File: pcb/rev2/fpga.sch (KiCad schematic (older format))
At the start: 45 parts, among them CN4 JTAG, IC1 XC6SLX9-3TQG144I, IC2 M25P80-VMN6P

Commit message: pcb wip
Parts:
- C10, C12, C13, C14, C15, C16, C18, C19, C20, C21, C22, C23, C24, C25, C3, C35, C36, C37, C38, C4, C40, C5, C6, C8, C9: footprint CAPC1608X87N -> Capacitors SMD:CAPC1608X87N
- C26, C39: footprint CAPC1608X90N -> Capacitors SMD:CAPC1608X90N
- R10, R11, R12, R13, R14, R15, R16, R17, R18, R20, R21, R7, R72, R8, R9: footprint RESC1608X55N -> Resistors SMD:RESC1608X55N

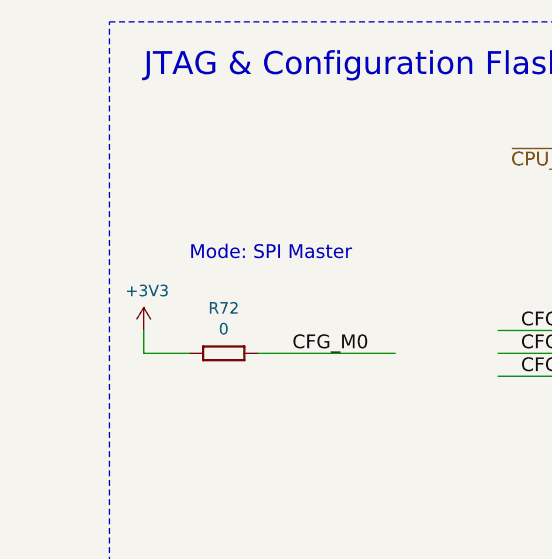
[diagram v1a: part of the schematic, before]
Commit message: Completed port to KiCad, passes DRC+LVS. NOT MANUFACTURED.
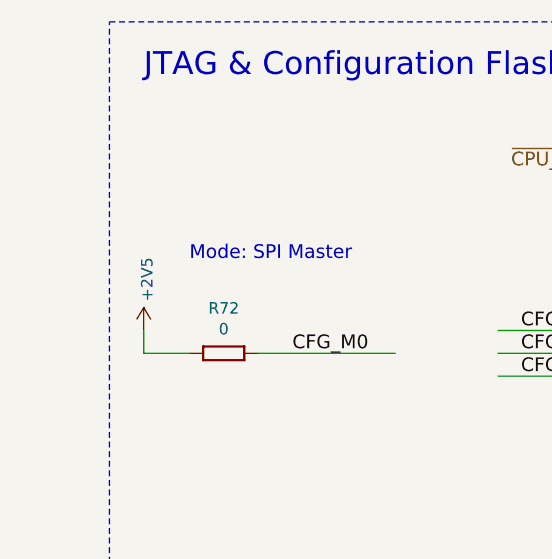
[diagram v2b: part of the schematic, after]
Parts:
- CN4: footprint (none) -> Pin_Headers:Pin_Header_Straight_1x06; Fieldname (none) -> Value
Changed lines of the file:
@@
 F 0 "CN4" H 6469 2175 50  0000 C CNN
 F 1 "JTAG" H 6469 2266 50  0000 C CNN
-F 2 "" H 6550 2650 50  0001 C CNN
+F 2 "Pin_Headers:Pin_Header_Straight_1x06" H 6550 2650 50  0001 C CNN
 F 3 "" H 6550 2650 50  0001 C CNN
+F 4 "Value" H 6550 2650 60  0001 C CNN "Fieldname"
 	1    6550 2650
 	-1   0    0    1
@@
 	1    0    0    -1
 $EndComp
-$Comp
-L +3V3 #PWR019
-U 1 1 5990096E
-P 1450 2250
-F 0 "#PWR019" H 1450 2100 50  0001 C CNN
-F 1 "+3V3" H 1465 2423 50  0000 C CNN
-F 2 "" H 1450 2250 50  0001 C CNN
-F 3 "" H 1450 2250 50  0001 C CNN
-	1    1450 2250
-	1    0    0    -1
-$EndComp
 Text Notes 1650 1950 0    60   ~ 0
 Mode: SPI Master
@@
 Text Notes 12450 10925 2    60   ~ 0
 FPGA
+$Comp
+L +2V5 #PWR019
+U 1 1 599ECA35
+P 1450 2250
+F 0 "#PWR019" H 1450 2100 50  0001 C CNN
+F 1 "+2V5" V 1465 2378 50  0000 L CNN
+F 2 "" H 1450 2250 50  0001 C CNN
+F 3 "" H 1450 2250 50  0001 C CNN
+	1    1450 2250
+	1    0    0    -1
+$EndComp
 $EndSCHEMATC

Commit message: axi4/zynq version: wip
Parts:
- C10, C12, C13, C15, C16, C18, C20, C21, C22, C23, C25, C3, C35, C36, C37, C38, C4, C40, C5, C8: symbol CC0603_100NF_50V_10%_X7R -> dsi_shield-rescue:CC0603_100NF_50V_10%_X7R-
- C14, C19, C24, C6, C9: symbol CC0603_1UF_50V_10%_X5R -> dsi_shield-rescue:CC0603_1UF_50V_10%_X5R-
- C26, C39: symbol CC0603_1NF_50V_5%_NP0 -> dsi_shield-rescue:CC0603_1NF_50V_5%_NP0-
- CN4: symbol CONN_01X06 -> dsi_shield-rescue:CONN_01X06-
- IC1: symbol XC6SLX9-3TQG144I -> dsi_shield-rescue:XC6SLX9-3TQG144I-
- IC2: symbol M25P80-VMN6P -> dsi_shield-rescue:M25P80-VMN6P-
- R10, R7, R8, R9: symbol R0603_3K3_1%_0.1W_100PPM -> dsi_shield-rescue:R0603_3K3_1%_0.1W_100PPM-
- R11, R12, R13, R14, R15, R16, R17, R18: symbol R0603_51R_1%_0.1W_100PPM -> dsi_shield-rescue:R0603_51R_1%_0.1W_100PPM-
- R20: symbol R0603_180R_1%_0.1W_100PPM -> dsi_shield-rescue:R0603_180R_1%_0.1W_100PPM-
- R21: symbol R0603_220R_1%_0.1W_100PPM -> dsi_shield-rescue:R0603_220R_1%_0.1W_100PPM-
- R72: symbol R0603_0R_JUMPER -> dsi_shield-rescue:R0603_0R_JUMPER-
